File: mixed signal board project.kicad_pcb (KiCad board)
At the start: 4 copper layers, 70.4 x 72.2 mm, 189 parts, among them J101 USB_B_Mini, J102 Conn_01x06_Pin, J201 8P8C_Shielded, J301 Conn_01x04_Pin, J401 AudioJack2_Ground, J402 Conn_01x04_Pin, J403 Screw_Terminal_01x03, J501 USB_B_Mini, J701 Conn_01x02_Socket, J801 Conn_01x02_Socket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

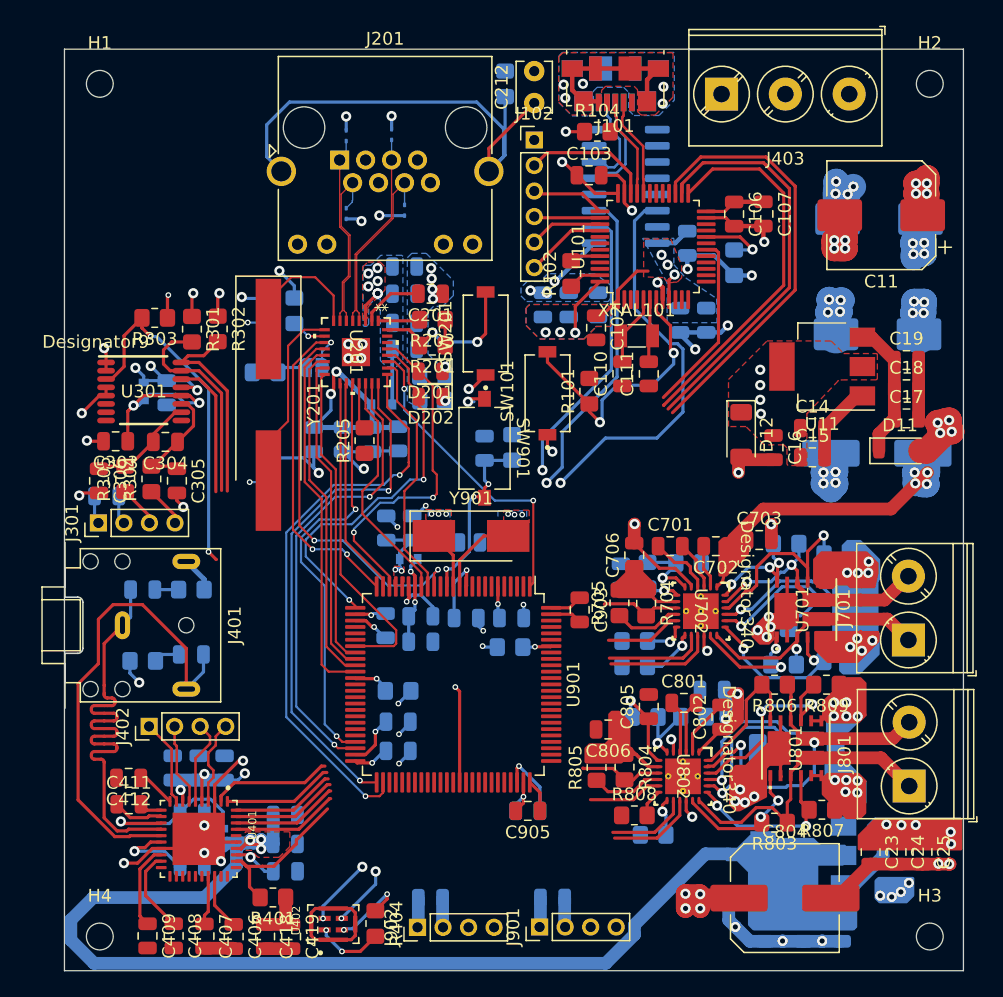
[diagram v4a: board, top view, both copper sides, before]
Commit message: All tracks routed, ERC done, waiting for PDN Analysis.
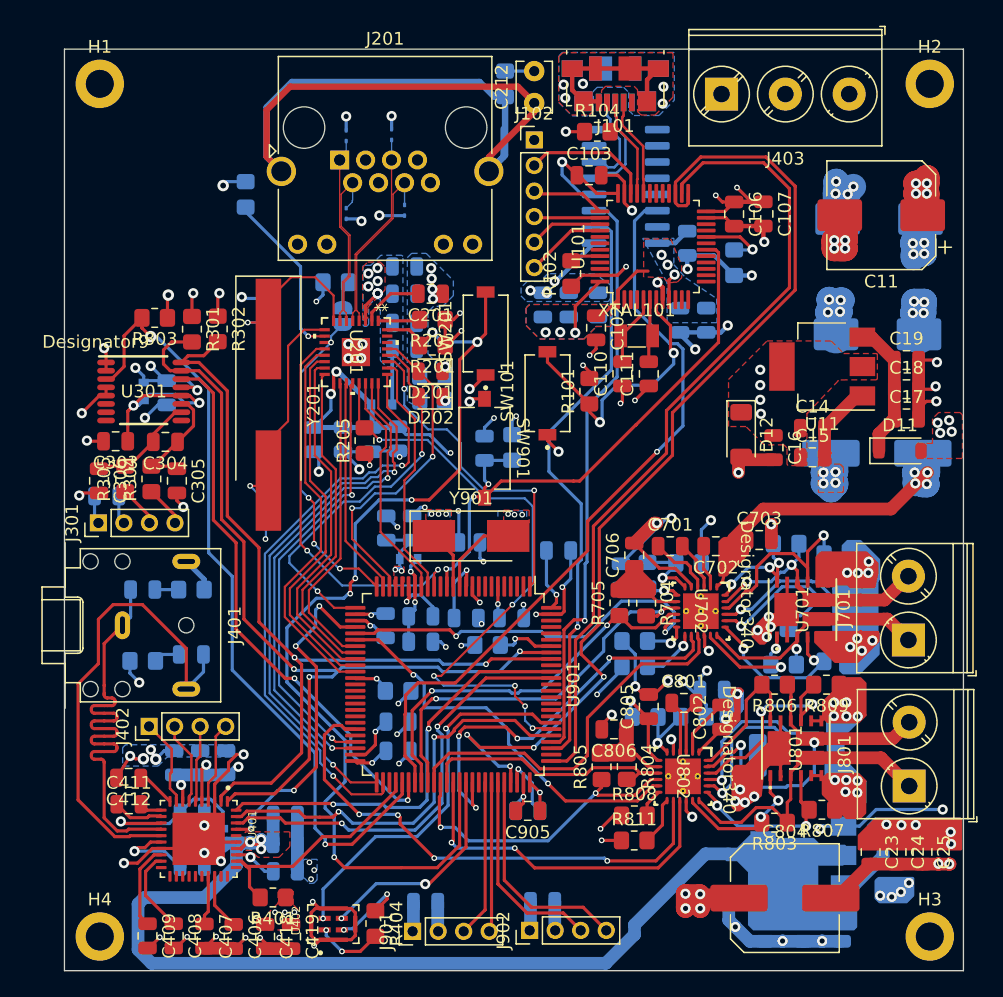
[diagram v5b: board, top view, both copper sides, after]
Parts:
- C903: moved to B.Cu
- H1, H2, H3, H4: footprint MountingHole:MountingHole_2.1mm -> MountingHole:MountingHole_2.2mm_M2_DIN965_Pad
- R811: moved to F.Cu
- moved C914 9.95 mm to (111.9, 124.3)
- moved J901 9.95 mm to (110.9, 126.6)
- moved R206 9.88 mm to (97.8, 68.9)
- moved R208 8.97 mm to (104.8, 75.7)
- moved C911 8.79 mm to (121.1, 124.2)
- moved J902 8.79 mm to (120.0, 126.5)
- moved C903 4.94 mm to (122.3, 96.8), turned to 0 degrees
- moved JP201 4.62 mm to (105.4, 78.4), turned to -90 degrees
- moved C206 3.22 mm to (99.4, 93.7), turned to 90 degrees
- moved R901 1.77 mm to (116.7, 104.2)
- moved R811 1.54 mm to (128.2, 119.5)
- moved C806 0.45 mm to (126.6, 110.8)
- moved C415 0.42 mm to (96.3, 113.4)
- moved C416 0.42 mm to (94.2, 113.4)
- moved C417 0.42 mm to (92.2, 113.4)
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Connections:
- J902 pad 3: /STM32F407/CAN_TX -> /STM32F407/CAN_RX
- J902 pad 4: /STM32F407/CAN_RX -> /STM32F407/CAN_TX
- U901 pad 30: /Motor_Driver1/SO -> /Motor_Driver2/SO_2
- U901 pad 31: /Motor_Driver2/SO_2 -> /Motor_Driver1/SO
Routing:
- net GND: track 253.7 -> 339.0 mm, vias 85 -> 127
- net Earth: track 0.00 -> 68.9 mm
- net /Ethernet/RESET_PHY: track 20.4 -> 81.7 mm, vias 3 -> 6
- net /ADC/SDA: track 25.6 -> 71.0 mm, vias 0 -> 3
- net /Ethernet/ETH_INT: track 3.66 -> 48.3 mm, vias 0 -> 6
- net /ADC/SCL: track 25.4 -> 67.4 mm, vias 0 -> 2
- net /ADC/RESET_ADC: track 27.8 -> 62.3 mm
- net /Motor_Driver1/EN: track 6.38 -> 40.6 mm, vias 0 -> 4
- net /ADC/~{DRDY}_ADC: track 10.8 -> 43.5 mm, vias 0 -> 2
- net /Debugger/JTCLK_F407: track 31.9 -> 64.0 mm
- net /Ethernet/RJ_45_SH: track 41.3 -> 70.0 mm
- net /STM32F407/CH340_~{RST}: track 30.9 -> 59.1 mm
- net /DAC adn MIC/SCLK_DAC: track 8.44 -> 34.2 mm, vias 0 -> 2
- net +3V3: track 118.2 -> 143.9 mm, vias 32 -> 48
- net /Motor_Driver1/SO: track 5.80 -> 31.2 mm, vias 0 -> 2
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- added copper zone on F.Cu, net +12V
- added copper zone on In2.Cu, net Earth

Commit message: schematic pages are reviewed
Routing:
- net GND: track 339.0 -> 305.0 mm, vias 127 -> 128
- net +12V: track 74.7 -> 48.6 mm, vias 38 -> 39
- net /STM32F407/CH340_TXD: track 46.5 -> 44.9 mm
- net /Debugger/JTMS_F407: track 80.0 -> 78.8 mm
- net /STM32F407/CH340_RXD: track 46.1 -> 45.5 mm
- added copper zone on B.Cu, net +12V
